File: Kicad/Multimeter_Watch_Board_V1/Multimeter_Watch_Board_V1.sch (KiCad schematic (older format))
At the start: 38 parts, among them J1 AudioJack3_Ground_renamedPins, J2 AudioJack3_Ground_renamedPins, J3 AudioJack3_Ground_renamedPins, J4 Conn_01x16_Female, J5 Conn_01x16_Female, U1 PCF85163-SO08, U2 AD8592, Y1 32kHz

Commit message: reset pullup
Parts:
- added R?: R, Resistor_SMD:R_0603_1608Metric_Pad1.05x0.95mm_HandSolder, symbol Device:R
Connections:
- net RESET: now also R?.2
- net VCC: now also R?.1
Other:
- note added: "Reset pullup\n"
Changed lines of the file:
@@
 EESchema Schematic File Version 4
-LIBS:Multimeter_Watch_Board_V1-cache
-EELAYER 26 0
+EELAYER 30 0
 EELAYER END
 $Descr A4 11693 8268
@@
 Wire Notes Line
 	11200 500  11200 6500
-Wire Notes Line
-	7000 6500 7000 4050
 $Comp
 L Device:C_Small C2
@@
 Wire Notes Line
 	4900 5400 7000 5400
-Wire Notes Line
-	4900 500  4900 5400
 Wire Wire Line
 	5750 4650 5900 4650
@@
 	-1   0    0    1
 $EndComp
+Text Notes 5300 5700 0    118  ~ 0
+Reset pullup\n
+Text Label 5450 6500 2    50   ~ 0
+RESET
+Text Label 6250 6500 0    50   ~ 0
+RESET
+Wire Wire Line
+	5850 6300 5850 6500
+$Comp
+L Device:R R?
+U 1 1 5F23EEDA
+P 5850 6150
+F 0 "R?" H 5920 6196 50  0000 L CNN
+F 1 "R" H 5920 6105 50  0000 L CNN
+F 2 "Resistor_SMD:R_0603_1608Metric_Pad1.05x0.95mm_HandSolder" V 5780 6150 50  0001 C CNN
+F 3 "~" H 5850 6150 50  0001 C CNN
+	1    5850 6150
+	1    0    0    -1
+$EndComp
+Connection ~ 5850 6500
+Wire Wire Line
+	5850 6500 6250 6500
+Wire Wire Line
+	5450 6500 5850 6500
+Wire Wire Line
+	5850 6000 5850 5850
+Wire Wire Line
+	5850 5850 6050 5850
+Text Label 6050 5850 0    50   ~ 0
+VCC
+Wire Notes Line
+	4900 6700 7000 6700
+Wire Notes Line
+	7000 4050 7000 6700
+Wire Notes Line
+	4900 500  4900 6700
 $EndSCHEMATC

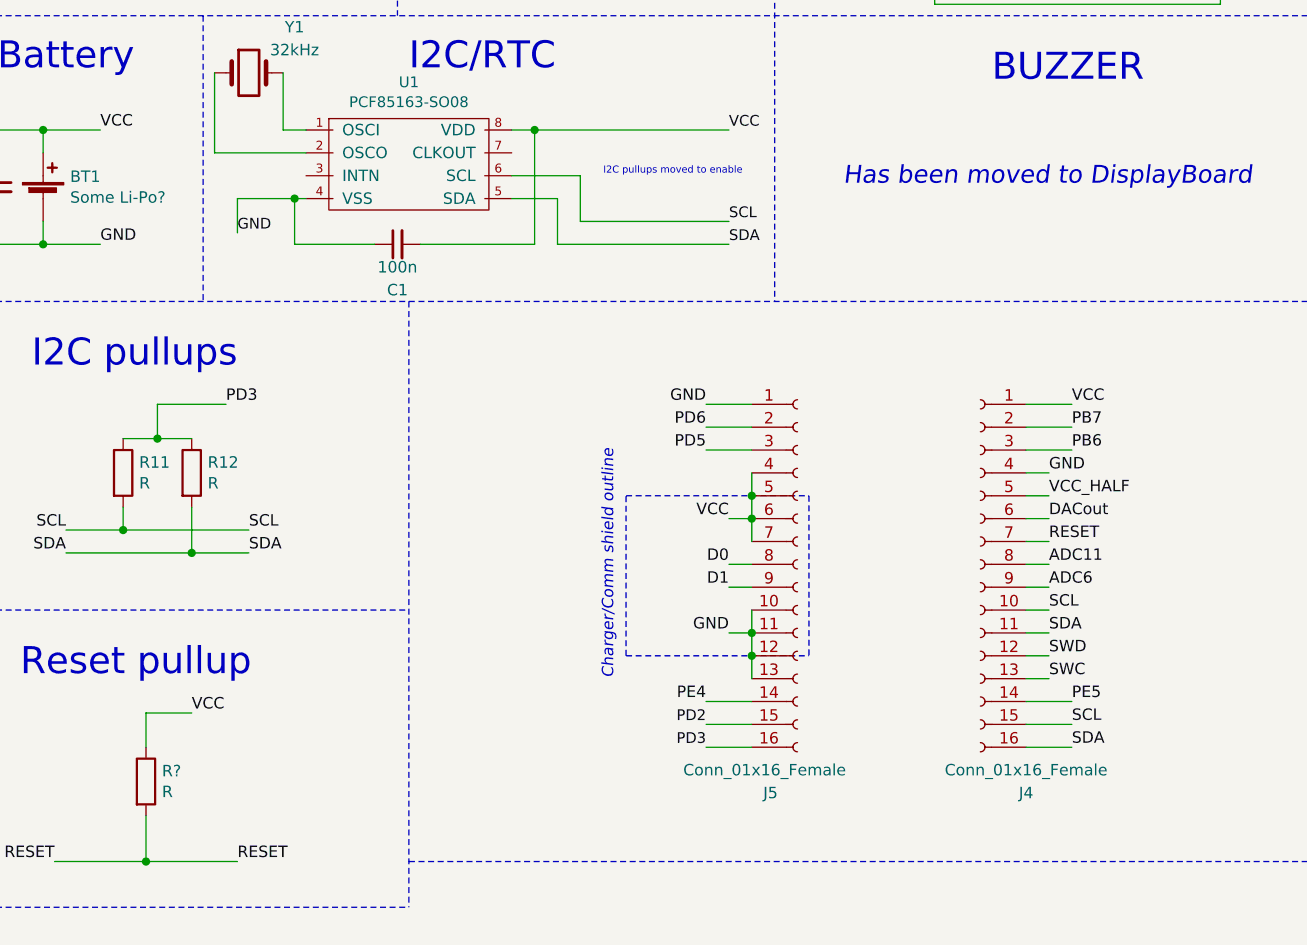
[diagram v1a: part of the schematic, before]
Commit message: group rlc tester pins on right header
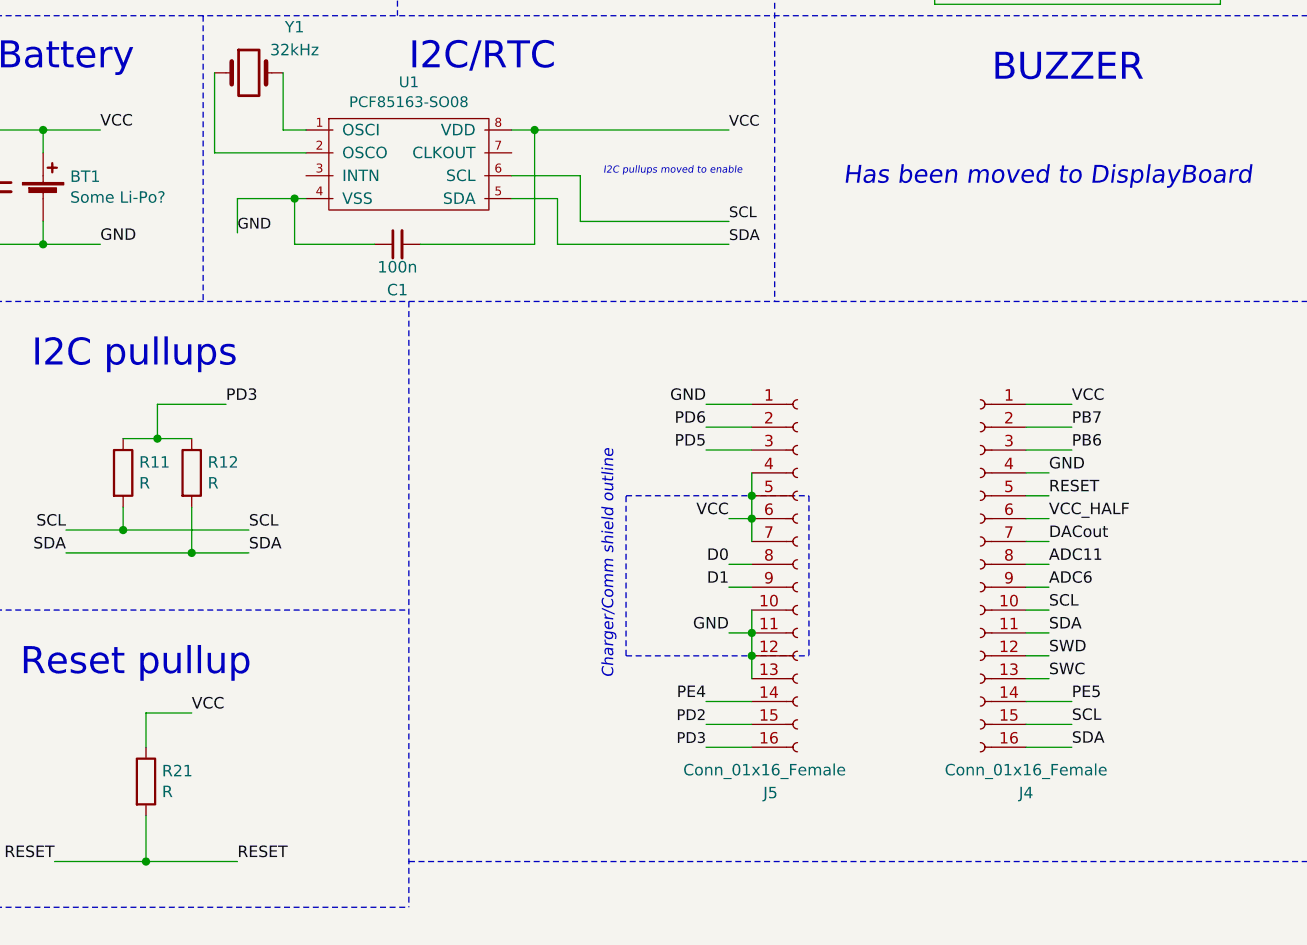
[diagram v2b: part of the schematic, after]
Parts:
- gave numbers to parts that had none: 1
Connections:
- net ADC3: now also J4.7 (Pin_7); no longer J4.6 (Pin_6)
- net RESET: now also J4.5 (Pin_5); no longer J4.7 (Pin_7)
- net VCC_HALF: now also J4.6 (Pin_6); no longer J4.5 (Pin_5)
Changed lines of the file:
@@
 Wire Wire Line
 	9800 5700 9700 5700
+Text Label 9800 4900 0    50   ~ 0
+RESET
+Text Label 9800 5000 0    50   ~ 0
+VCC_HALF
 Text Label 9800 5100 0    50   ~ 0
-RESET
-Text Label 9800 4900 0    50   ~ 0
-VCC_HALF
-Text Label 9800 5000 0    50   ~ 0
 DACout
 Text Label 9800 5700 0    50   ~ 0
@@
 Wire Wire Line
 	7550 3300 8400 3300
-Text Notes 7850 3500 0    31   ~ 0
+Text Notes 7850 3500 0    31   Italic 0
 I2C pullups moved to enable
 Text Label 5500 5050 2    50   ~ 0
@@
 	5850 6300 5850 6500
 $Comp
-L Device:R R?
+L Device:R R21
 U 1 1 5F23EEDA
 P 5850 6150
-F 0 "R?" H 5920 6196 50  0000 L CNN
+F 0 "R21" H 5920 6196 50  0000 L CNN
 F 1 "R" H 5920 6105 50  0000 L CNN
 F 2 "Resistor_SMD:R_0603_1608Metric_Pad1.05x0.95mm_HandSolder" V 5780 6150 50  0001 C CNN

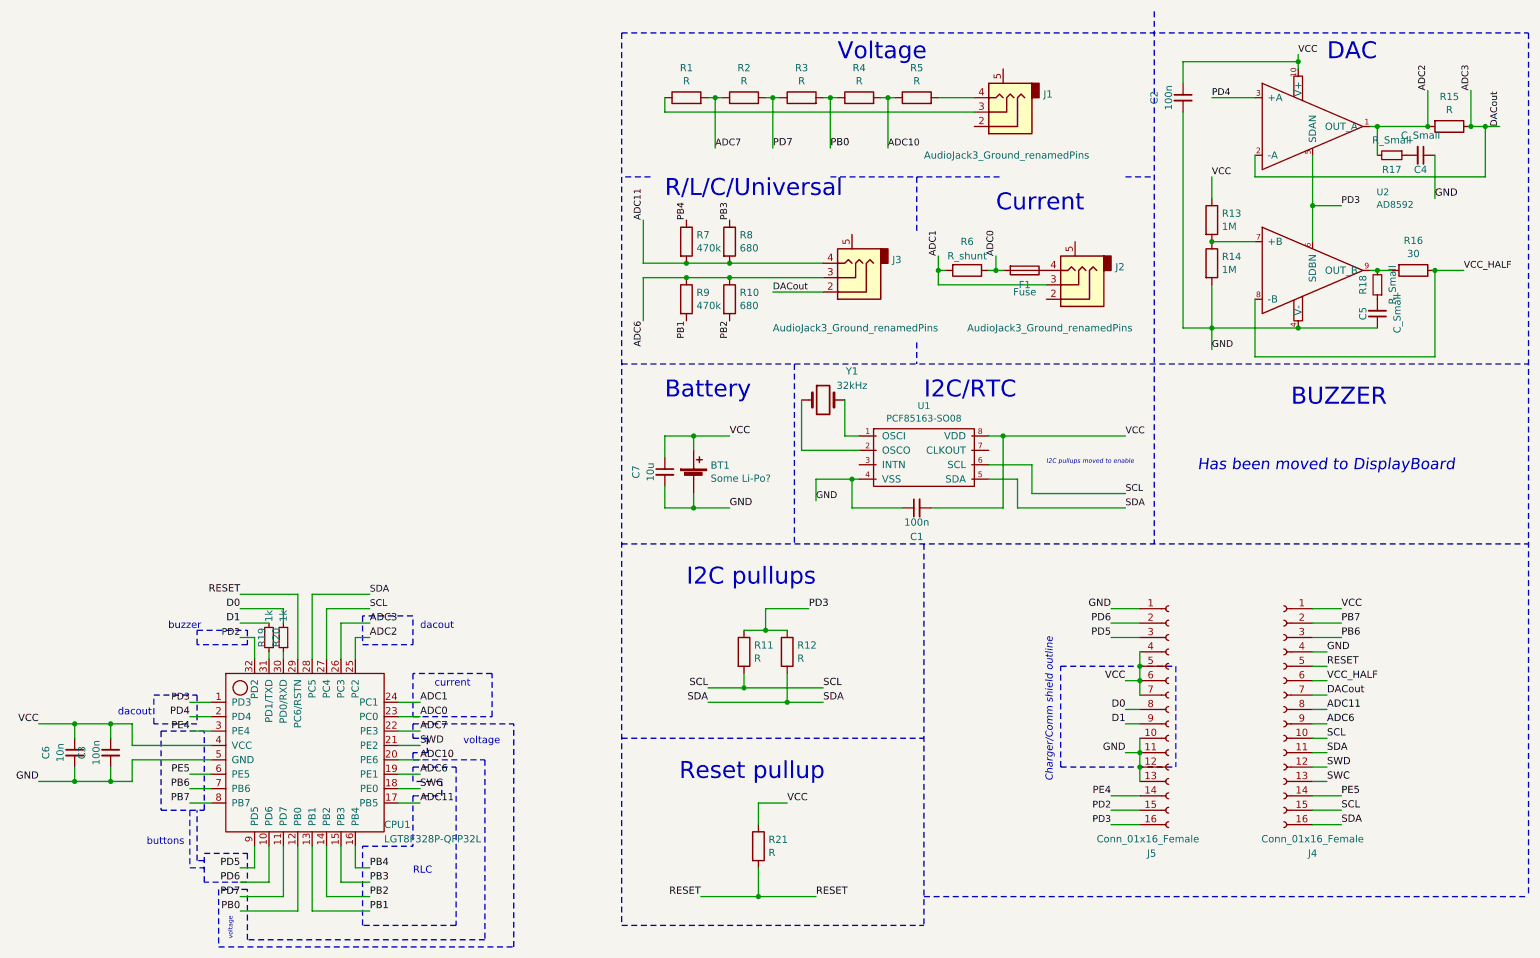
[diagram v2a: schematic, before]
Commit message: Add values for components in schematics; implement voltmeter; fix the bug where the watch goes sleep when the stopwatch is running; try implementing ohmmeter; allow the user to exit power supply app; show the output of keyboard test on display; implement averager
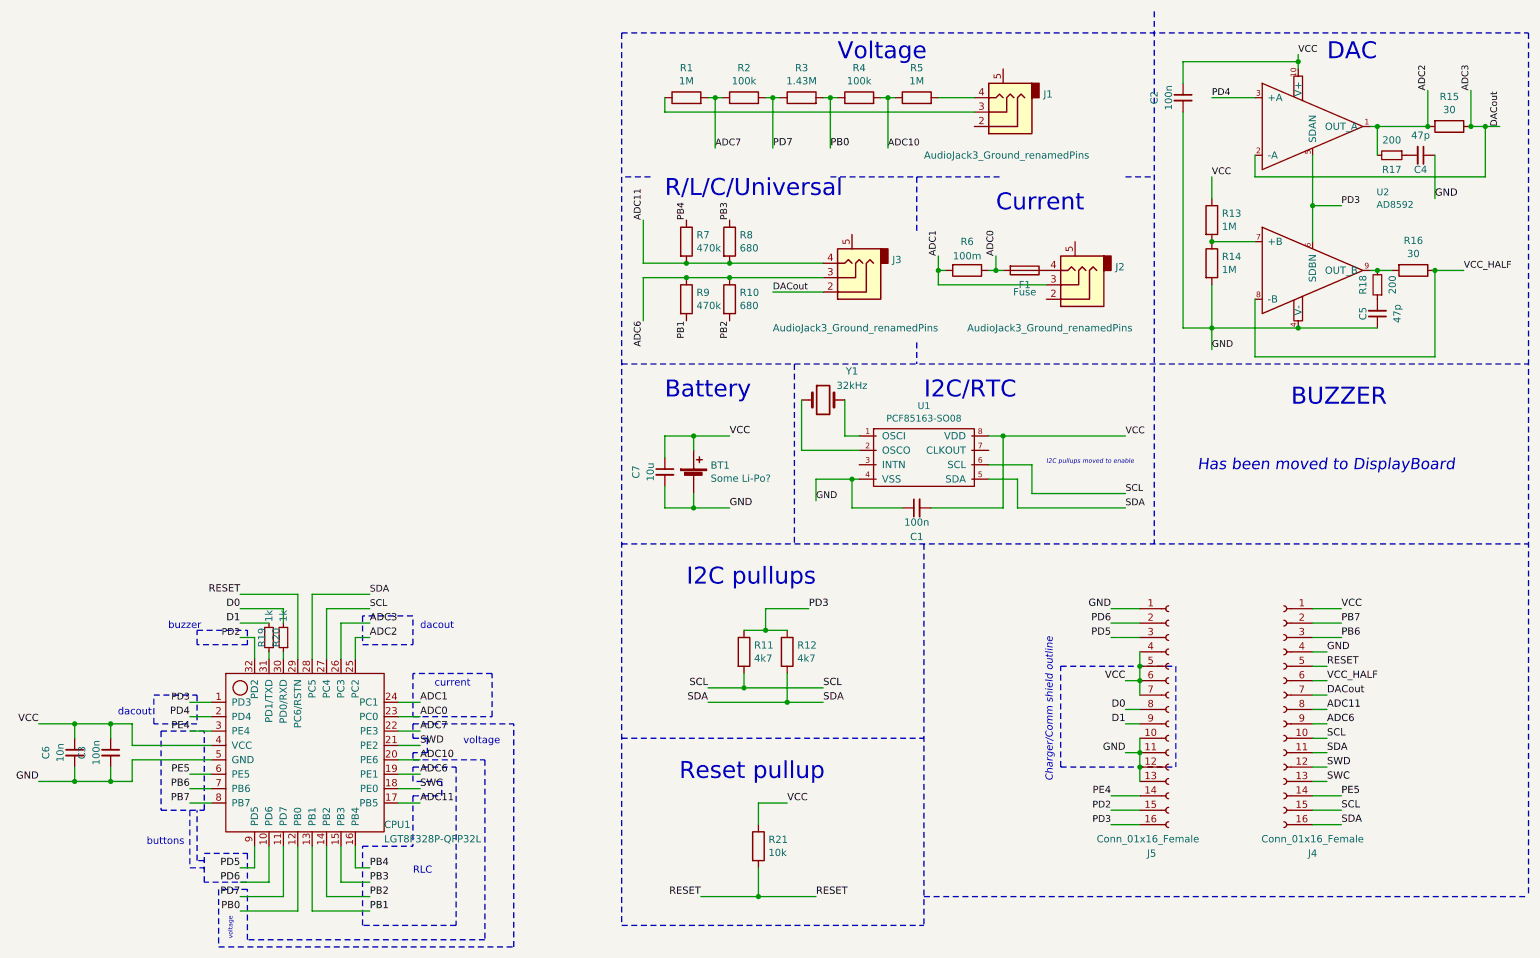
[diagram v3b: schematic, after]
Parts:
- C4, C5: value C_Small -> 47p
- R1, R5: value R -> 1M
- R11, R12: value R -> 4k7
- R15: value R -> 30
- R17, R18: value R_Small -> 200
- R2, R4: value R -> 100k
- R21: value R -> 10k
- R3: value R -> 1.43M
- R6: value R_shunt -> 100m
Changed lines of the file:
@@
 EESchema Schematic File Version 4
-EELAYER 30 0
+LIBS:Multimeter_Watch_Board_V1-cache
+EELAYER 26 0
 EELAYER END
 $Descr A4 11693 8268
@@
 P 6950 950
 F 0 "R5" V 7157 950 50  0000 C CNN
-F 1 "R" V 7066 950 50  0000 C CNN
+F 1 "1M" V 7066 950 50  0000 C CNN
 F 2 "Resistor_SMD:R_0805_2012Metric_Pad1.15x1.40mm_HandSolder" V 6880 950 50  0001 C CNN
 F 3 "~" H 6950 950 50  0001 C CNN
@@
 P 6550 950
 F 0 "R4" V 6757 950 50  0000 C CNN
-F 1 "R" V 6666 950 50  0000 C CNN
+F 1 "100k" V 6666 950 50  0000 C CNN
 F 2 "Resistor_SMD:R_0805_2012Metric_Pad1.15x1.40mm_HandSolder" V 6480 950 50  0001 C CNN
 F 3 "~" H 6550 950 50  0001 C CNN
@@
 P 6150 950
 F 0 "R3" V 6357 950 50  0000 C CNN
-F 1 "R" V 6266 950 50  0000 C CNN
+F 1 "1.43M" V 6266 950 50  0000 C CNN
 F 2 "Resistor_SMD:R_0805_2012Metric_Pad1.15x1.40mm_HandSolder" V 6080 950 50  0001 C CNN
 F 3 "~" H 6150 950 50  0001 C CNN
@@
 P 5350 950
 F 0 "R1" V 5557 950 50  0000 C CNN
-F 1 "R" V 5466 950 50  0000 C CNN
+F 1 "1M" V 5466 950 50  0000 C CNN
 F 2 "Resistor_SMD:R_0805_2012Metric_Pad1.15x1.40mm_HandSolder" V 5280 950 50  0001 C CNN
 F 3 "~" H 5350 950 50  0001 C CNN
@@
 P 5750 950
 F 0 "R2" V 5957 950 50  0000 C CNN
-F 1 "R" V 5866 950 50  0000 C CNN
+F 1 "100k" V 5866 950 50  0000 C CNN
 F 2 "Resistor_SMD:R_0805_2012Metric_Pad1.15x1.40mm_HandSolder" V 5680 950 50  0001 C CNN
 F 3 "~" H 5750 950 50  0001 C CNN
@@
 P 7300 2150
 F 0 "R6" V 7100 2150 50  0000 C CNN
-F 1 "R_shunt" V 7200 2150 50  0000 C CNN
+F 1 "100m" V 7200 2150 50  0000 C CNN
 F 2 "Resistor_SMD:R_2512_6332Metric_Pad1.52x3.35mm_HandSolder" V 7230 2150 50  0001 C CNN
 F 3 "~" H 7300 2150 50  0001 C CNN
@@
 P 5750 4800
 F 0 "R11" H 5820 4846 50  0000 L CNN
-F 1 "R" H 5820 4755 50  0000 L CNN
+F 1 "4k7" H 5820 4755 50  0000 L CNN
 F 2 "Resistor_SMD:R_0603_1608Metric_Pad1.05x0.95mm_HandSolder" V 5680 4800 50  0001 C CNN
 F 3 "~" H 5750 4800 50  0001 C CNN
@@
 P 6050 4800
 F 0 "R12" H 6120 4846 50  0000 L CNN
-F 1 "R" H 6120 4755 50  0000 L CNN
+F 1 "4k7" H 6120 4755 50  0000 L CNN
 F 2 "Resistor_SMD:R_0603_1608Metric_Pad1.05x0.95mm_HandSolder" V 5980 4800 50  0001 C CNN
 F 3 "~" H 6050 4800 50  0001 C CNN
@@
 P 10650 1150
 F 0 "R15" V 10443 1150 50  0000 C CNN
-F 1 "R" V 10534 1150 50  0000 C CNN
+F 1 "30" V 10534 1150 50  0000 C CNN
 F 2 "Resistor_SMD:R_2512_6332Metric_Pad1.52x3.35mm_HandSolder" V 10580 1150 50  0001 C CNN
 F 3 "~" H 10650 1150 50  0001 C CNN
@@
 P 10450 1350
 F 0 "C4" V 10550 1350 50  0000 C CNN
-F 1 "C_Small" V 10312 1350 50  0000 C CNN
+F 1 "47p" V 10312 1350 50  0000 C CNN
 F 2 "Capacitor_SMD:C_0805_2012Metric_Pad1.15x1.40mm_HandSolder" H 10450 1350 50  0001 C CNN
 F 3 "~" H 10450 1350 50  0001 C CNN
@@
 P 10250 1350
 F 0 "R17" V 10350 1350 50  0000 C CNN
-F 1 "R_Small" V 10145 1350 50  0000 C CNN
+F 1 "200" V 10145 1350 50  0000 C CNN
 F 2 "Resistor_SMD:R_0805_2012Metric_Pad1.15x1.40mm_HandSolder" H 10250 1350 50  0001 C CNN
 F 3 "~" H 10250 1350 50  0001 C CNN
@@
 P 10150 2450
 F 0 "C5" V 10250 2450 50  0000 C CNN
-F 1 "C_Small" V 10012 2450 50  0000 C CNN
+F 1 "47p" V 10012 2450 50  0000 C CNN
 F 2 "Capacitor_SMD:C_0805_2012Metric_Pad1.15x1.40mm_HandSolder" H 10150 2450 50  0001 C CNN
 F 3 "~" H 10150 2450 50  0001 C CNN
@@
 P 10150 2250
 F 0 "R18" V 10250 2250 50  0000 C CNN
-F 1 "R_Small" V 10045 2250 50  0000 C CNN
+F 1 "200" V 10045 2250 50  0000 C CNN
 F 2 "Resistor_SMD:R_0805_2012Metric_Pad1.15x1.40mm_HandSolder" H 10150 2250 50  0001 C CNN
 F 3 "~" H 10150 2250 50  0001 C CNN
@@
 P 5850 6150
 F 0 "R21" H 5920 6196 50  0000 L CNN
-F 1 "R" H 5920 6105 50  0000 L CNN
+F 1 "10k" H 5920 6105 50  0000 L CNN
 F 2 "Resistor_SMD:R_0603_1608Metric_Pad1.05x0.95mm_HandSolder" V 5780 6150 50  0001 C CNN
 F 3 "~" H 5850 6150 50  0001 C CNN
